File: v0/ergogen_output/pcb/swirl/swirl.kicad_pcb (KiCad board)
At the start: 2 copper layers, 127.8 x 85 mm, 66 parts

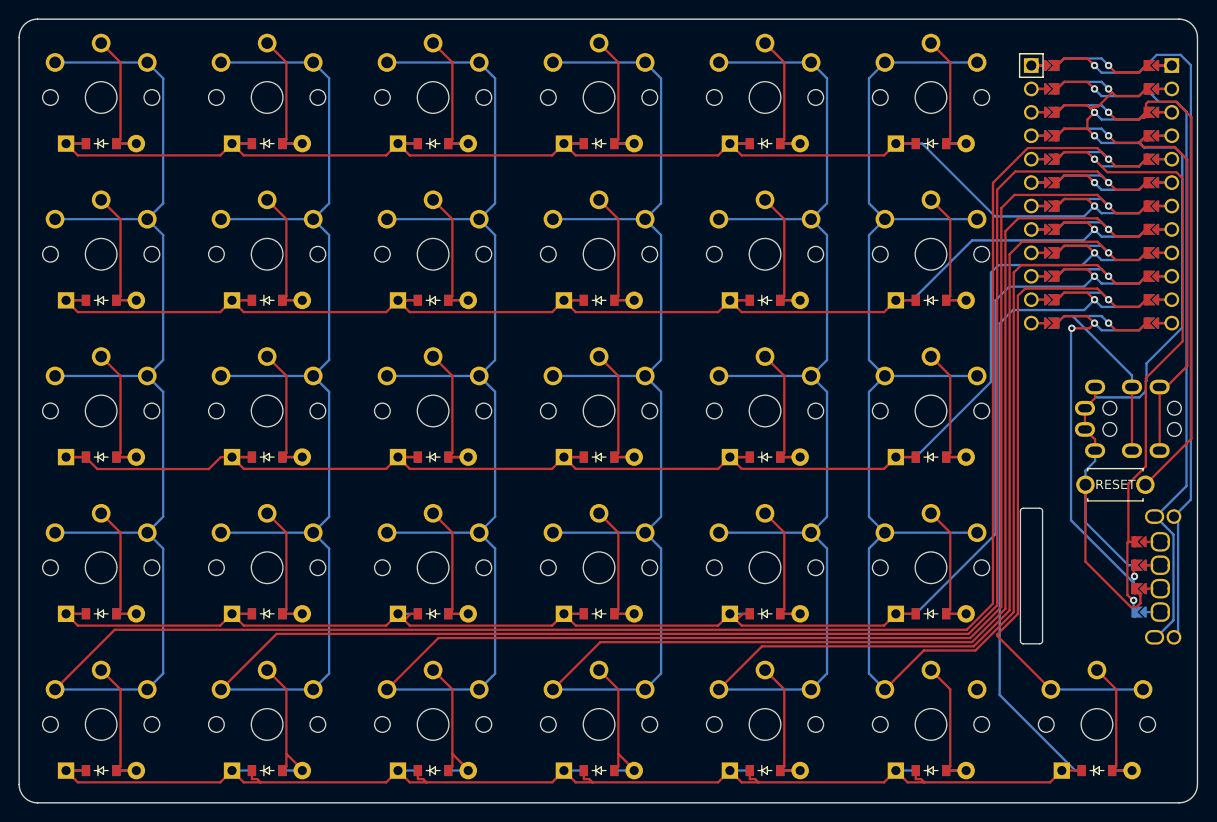
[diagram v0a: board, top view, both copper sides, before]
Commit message: fix 90 degree bend, general cleanup
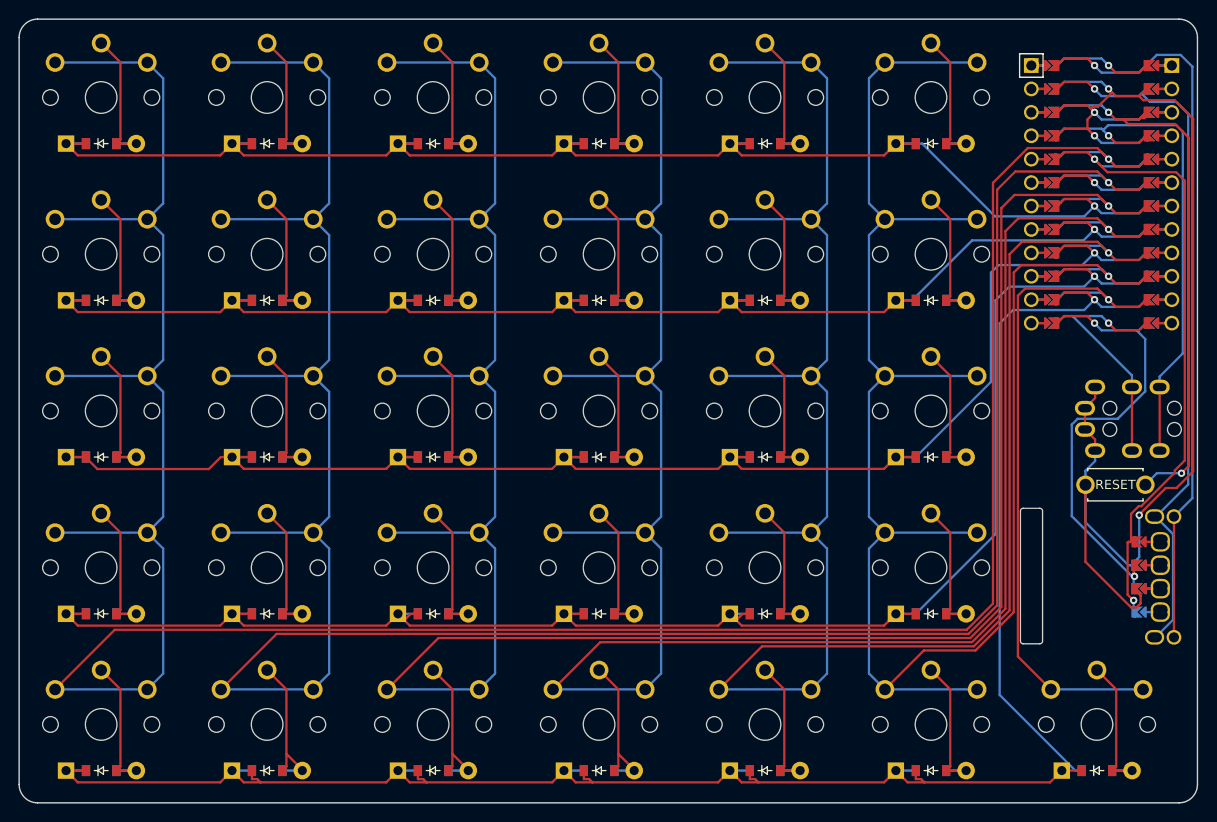
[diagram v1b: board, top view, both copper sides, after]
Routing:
- net GND: track 119.7 -> 139.2 mm, vias 3 -> 4
- net MISO: track 190.0 -> 200.0 mm
- net VCC: track 50.4 -> 55.7 mm
- net P7: track 183.9 -> 179.3 mm
- net P9: track 47.0 -> 49.7 mm, vias 3 -> 2
- net MOSI: track 77.6 -> 75.8 mm
- net P8: track 218.1 -> 217.1 mm
- net P1: track 81.4 -> 80.4 mm
- net RST: track 60.0 -> 60.5 mm, vias 1 -> 2

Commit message: Add drill files, make serial component use serial pin
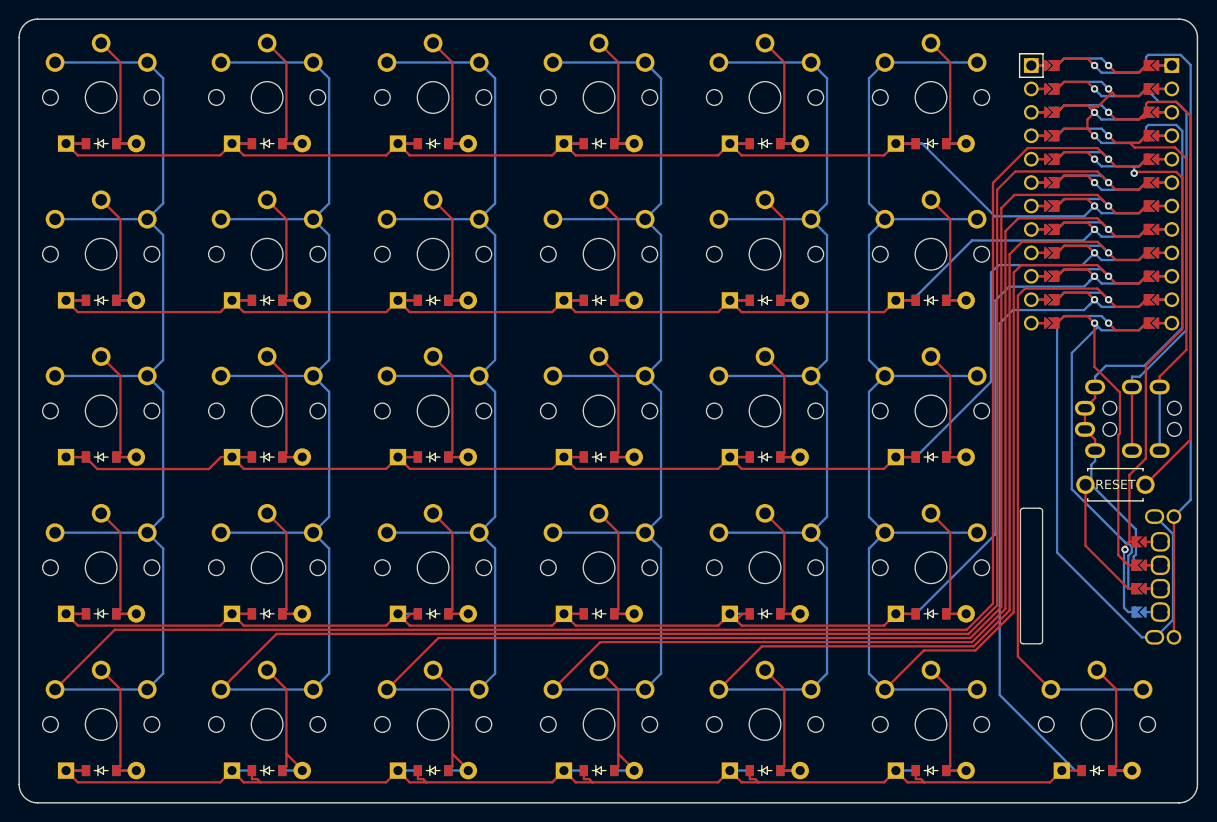
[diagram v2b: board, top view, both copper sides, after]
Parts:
- MCU1: moved to B.Cu
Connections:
- EN1 pad S2: P0 -> P10
- TRRS1 pad 3: P10 -> P0
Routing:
- net P10: track 28.2 -> 65.1 mm
- net GND: track 139.2 -> 115.0 mm, vias 4 -> 3
- net P9: track 49.7 -> 72.8 mm, vias 2 -> 1
- net P0: track 77.0 -> 56.3 mm
- net VCC: track 55.7 -> 50.6 mm
- net SDA: track 72.5 -> 68.8 mm, vias 2 -> 3
- net P7: track 179.3 -> 182.1 mm
- net P8: track 217.1 -> 218.9 mm
- net P1: track 80.4 -> 81.2 mm
- net RST: track 60.5 -> 59.9 mm, vias 2 -> 1

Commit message: fix some wiring, add some graphics, move some stuff to more convenient palces
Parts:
- MCU1: moved to F.Cu
- moved B1 3.00 mm to (110.0, -29.0)
- moved TRRS1 3.00 mm to (118.0, -35.0)
- moved EN1 2.20 mm to (109.5, -18.2)
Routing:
- net GND: track 115.0 -> 156.1 mm
- net P0: track 56.3 -> 75.6 mm
- net P9: track 72.8 -> 54.1 mm, vias 1 -> 2
- net P1: track 81.2 -> 96.6 mm
- net MISO: track 200.0 -> 214.0 mm
- net RST: track 59.9 -> 73.7 mm, vias 1 -> 2
- net SCL: track 12.0 -> 23.5 mm
- net RAW: track 10.9 -> 21.8 mm
- net MOSI: track 75.8 -> 86.5 mm
- net P8: track 218.9 -> 229.5 mm
- net P4: track 155.8 -> 166.2 mm
- net SCLK: track 220.1 -> 230.6 mm
- net P21: track 300.5 -> 310.9 mm
- net P20: track 281.1 -> 291.5 mm
- net P19: track 261.0 -> 271.4 mm
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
